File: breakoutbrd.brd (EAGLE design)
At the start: 72.4 x 82.5 mm, 6 parts

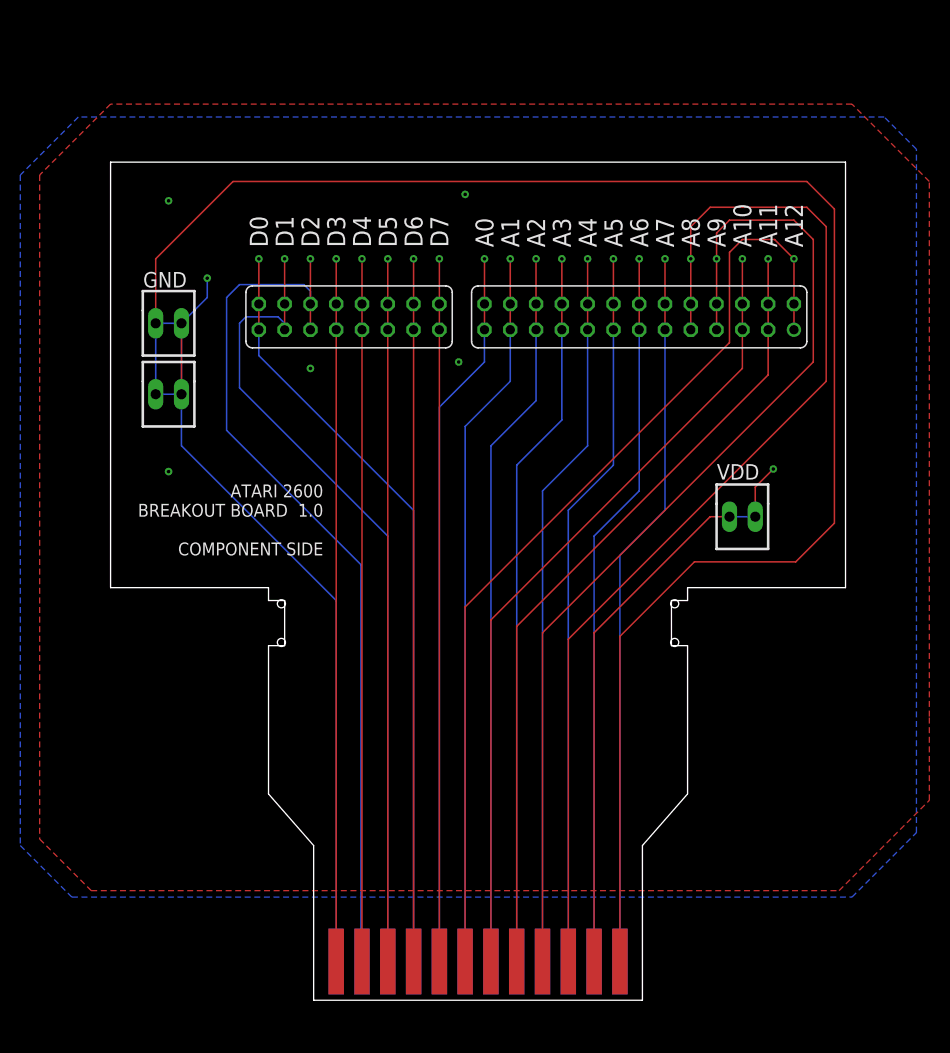
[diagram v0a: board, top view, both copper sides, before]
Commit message: Moved all components to land on 0.1" spacing, even between components. Makes soldering of all pins over a breadboard possible.
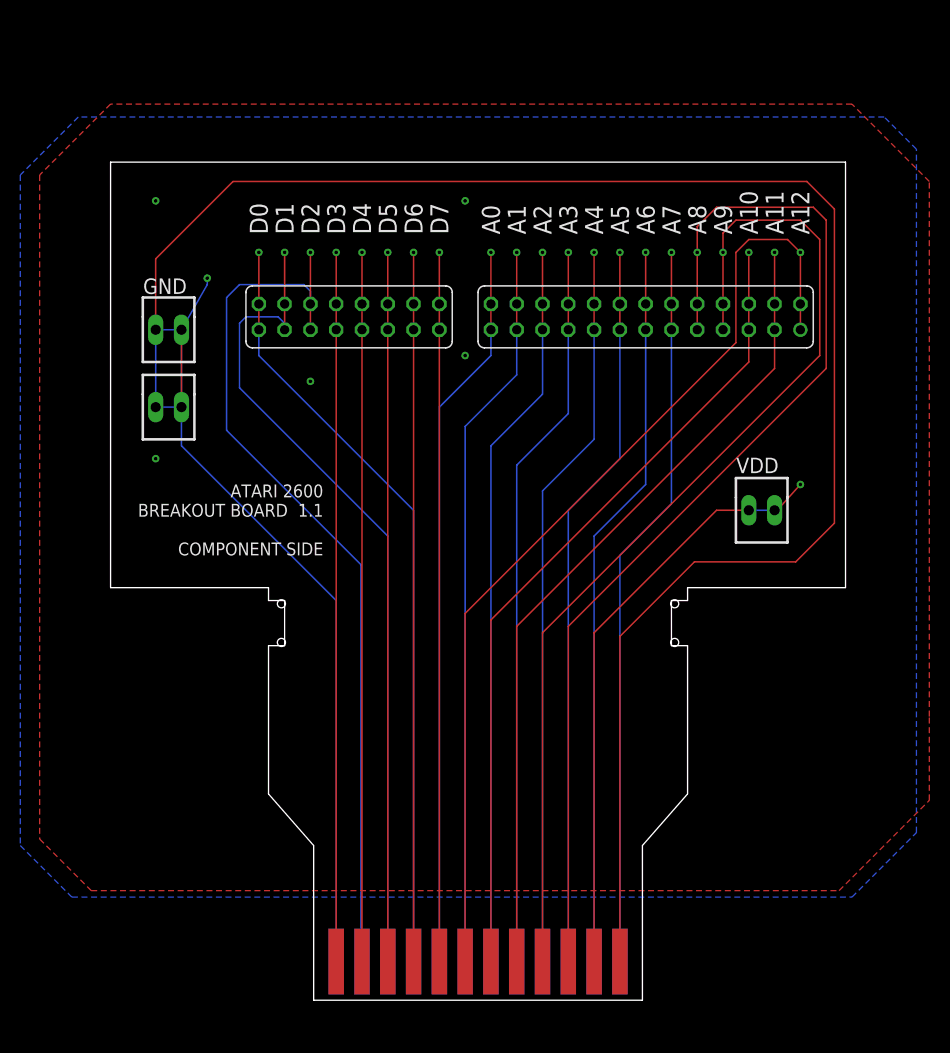
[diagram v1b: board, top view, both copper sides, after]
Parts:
- moved VDD 2.01 mm to (64.8, 48.3)
- moved GND1 1.27 mm to (6.35, 58.4)
- moved SV2 0.64 mm to (53.3, 67.3)
- moved GND 0.63 mm to (6.35, 66.0)
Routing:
- net GND: track 259.9 -> 261.5 mm
- net CADDR7: track 71.1 -> 72.0 mm
- net CADDR6: track 71.1 -> 72.0 mm
- net CADDR11: track 79.5 -> 80.4 mm
- net CADDR10: track 79.5 -> 80.4 mm
- net CADDR5: track 71.1 -> 72.0 mm
- net CADDR4: track 71.1 -> 72.0 mm
- net CADDR2: track 71.1 -> 72.0 mm
- net CADDR1: track 71.1 -> 72.0 mm
- net CADDR0: track 71.1 -> 72.0 mm
- net CADDR3: track 71.1 -> 72.0 mm
- net CADDR12: track 95.3 -> 95.9 mm
- net CDATA7: track 69.2 -> 69.8 mm
- net CDATA6: track 69.2 -> 69.8 mm
- net CDATA5: track 69.2 -> 69.8 mm
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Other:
- board text added: "ATARI 2600 BREAKOUT BOARD 1.1 COMPONENT SIDE"
- board text removed: "ATARI 2600 BREAKOUT BOARD 1.0 COMPONENT SIDE"

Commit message: optional cartridge connector added to pcb
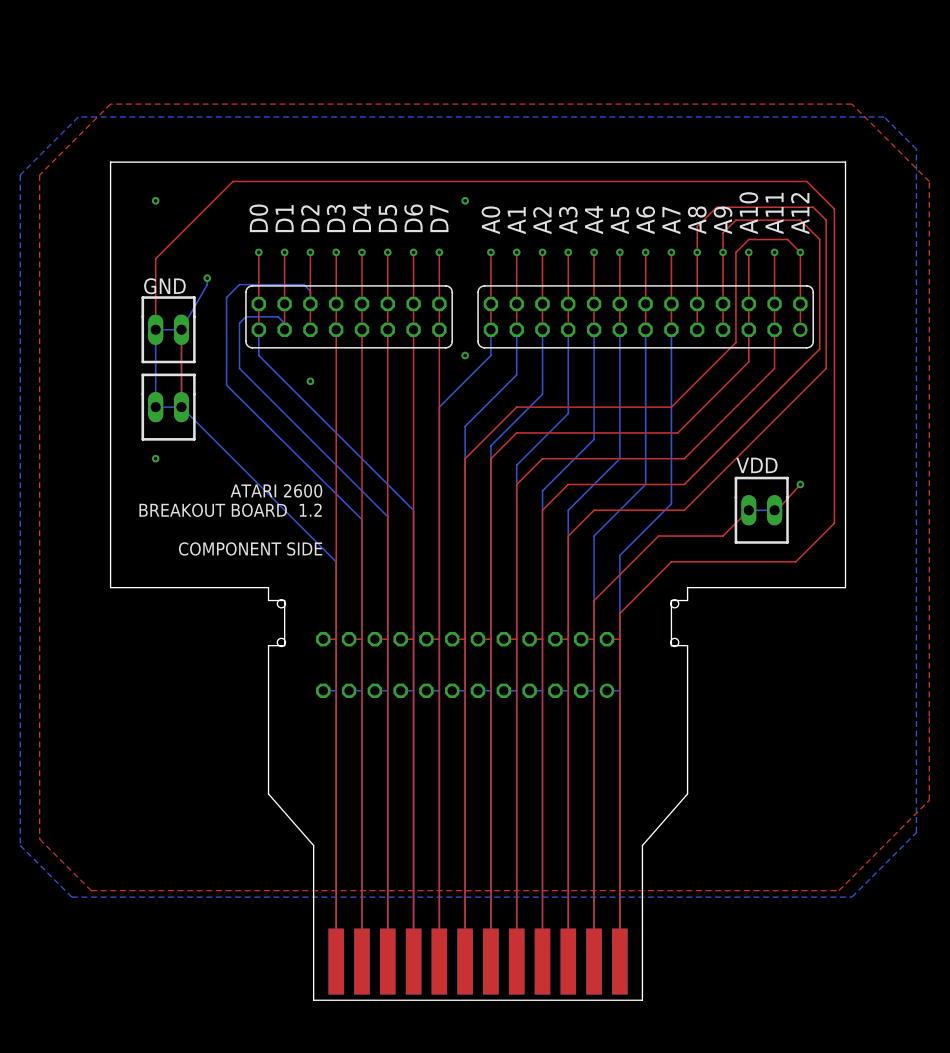
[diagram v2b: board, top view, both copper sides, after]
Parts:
- added U$1: EBC12DCWN, a26board:EBC12DCWN
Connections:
- net CADDR0: now also U$1.8
- net CADDR1: now also U$1.7
- net CADDR10: now also U$1.19
- net CADDR11: now also U$1.20
- net CADDR12: now also U$1.18
- net CADDR2: now also U$1.6
- net CADDR3: now also U$1.5
- net CADDR4: now also U$1.4
- net CADDR5: now also U$1.3
- net CADDR6: now also U$1.2
- net CADDR7: now also U$1.1
- net CADDR8: now also U$1.22
- net CADDR9: now also U$1.21
- net CDATA0: now also U$1.9
- net CDATA1: now also U$1.10
- net CDATA2: now also U$1.11
- net CDATA3: now also U$1.13
- net CDATA4: now also U$1.14
- net CDATA5: now also U$1.15
- net CDATA6: now also U$1.16
- net CDATA7: now also U$1.17
- net GND: now also U$1.12, U$1.24
- net VDD: now also U$1.23
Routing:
- net CADDR10: track 80.4 -> 90.9 mm
- net CADDR12: track 95.9 -> 106.1 mm
- net CADDR11: track 80.4 -> 89.8 mm
- net CADDR9: track 102.8 -> 110.8 mm
- net CADDR8: track 107.7 -> 114.2 mm
- net GND: track 261.5 -> 265.3 mm
- net VDD: track 58.8 -> 62.0 mm
- net CDATA7: track 69.8 -> 71.1 mm
- net CDATA0: track 76.2 -> 77.4 mm
- net CADDR4: track 72.0 -> 73.2 mm
- net CADDR3: track 72.0 -> 73.2 mm
- net CADDR2: track 72.0 -> 73.2 mm
- net CADDR1: track 72.0 -> 73.2 mm
- net CADDR0: track 72.0 -> 73.2 mm
- net CDATA6: track 69.8 -> 71.1 mm
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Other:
- board text added: "ATARI 2600 BREAKOUT BOARD 1.2 COMPONENT SIDE"
- board text added: "CARTRIDGE"
- board text removed: "ATARI 2600 BREAKOUT BOARD 1.1 COMPONENT SIDE"

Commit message: Upright cartridge connector, work in progress
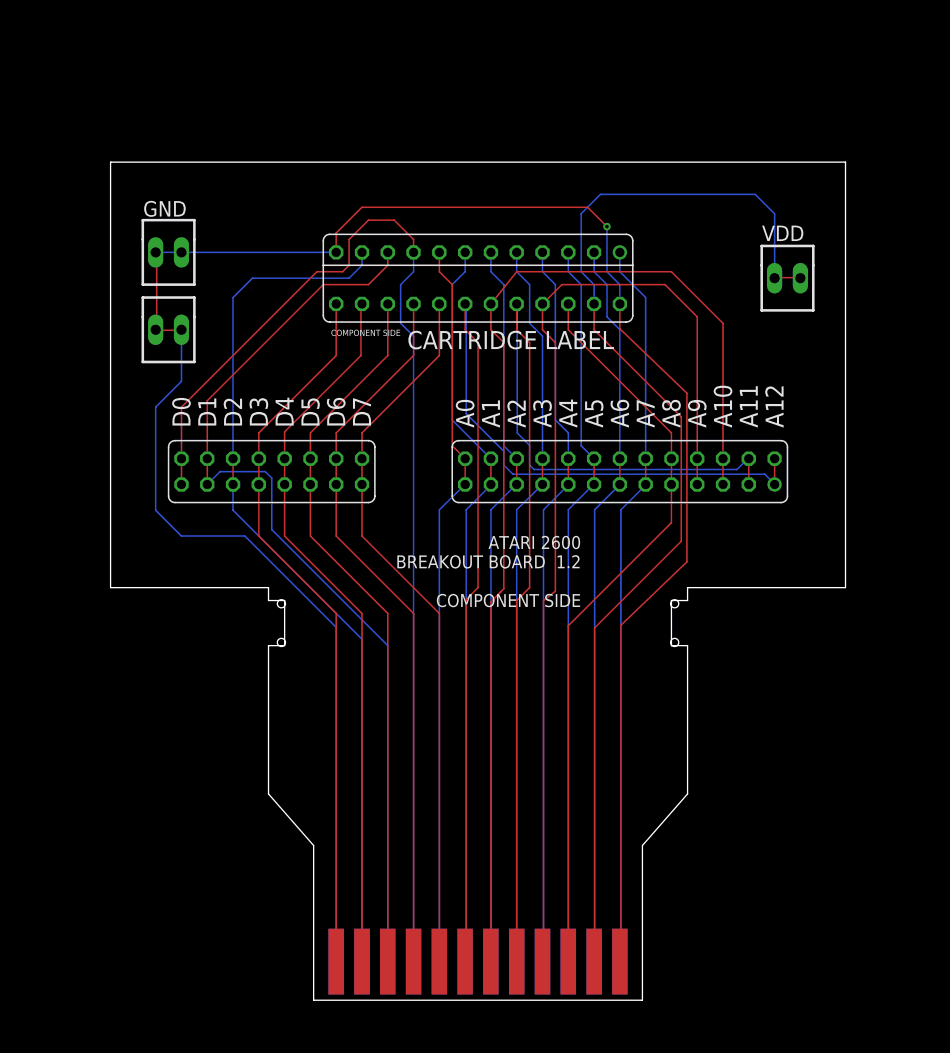
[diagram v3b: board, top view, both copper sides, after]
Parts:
- moved U$1 38.1 mm to (36.8, 71.1), flipped to the top, turned to 180 degrees
- moved VDD 23.0 mm to (67.3, 71.1)
- moved SV1 17.0 mm to (16.5, 52.1)
- moved SV2 15.5 mm to (50.8, 52.1)
- moved GND1 7.62 mm to (6.35, 66.0)
- moved GND 7.62 mm to (6.35, 73.7)
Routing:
- net GND: track 265.3 -> 211.4 mm, vias 6 -> 1
- net VDD: track 62.0 -> 110.9 mm, vias 1 -> 0
- net CADDR8: track 114.2 -> 73.2 mm, vias 1 -> 0
- net CDATA0: track 77.4 -> 112.6 mm, vias 1 -> 0
- net CADDR10: track 90.9 -> 108.6 mm, vias 1 -> 0
- net CADDR11: track 89.8 -> 107.0 mm, vias 1 -> 0
- net CADDR9: track 110.8 -> 99.8 mm, vias 1 -> 0
- net CDATA1: track 83.4 -> 92.3 mm, vias 1 -> 0
- net CADDR12: track 106.1 -> 113.4 mm, vias 1 -> 0
- net CDATA2: track 90.2 -> 86.0 mm, vias 1 -> 0
- net CADDR3: track 73.2 -> 72.0 mm, vias 1 -> 0
- net CADDR0: track 73.2 -> 72.0 mm, vias 1 -> 0
- net CADDR5: track 73.2 -> 72.0 mm, vias 1 -> 0
- net CADDR2: track 73.2 -> 72.0 mm, vias 1 -> 0
- net CADDR6: track 73.2 -> 72.0 mm, vias 1 -> 0
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- removed copper zone on layer 1, net GND
- removed copper zone on layer 16, net GND
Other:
- board text added: "CARTRIDGE LABEL"
- board text removed: "CARTRIDGE"

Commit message: More adjustments
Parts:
- moved VDD 5.08 mm to (67.3, 66.0)
- moved GND1 2.54 mm to (6.35, 63.5)
- moved GND 2.54 mm to (6.35, 71.1)
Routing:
- net CDATA2: track 86.0 -> 81.5 mm
- net VDD: track 110.9 -> 113.4 mm
- net GND: track 211.4 -> 209.7 mm

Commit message: working on double sided edge connectors, work in progrss.
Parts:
- J1: device a26board:MED_NOHOLE -> a26board:BREAKOUT_BOARD
- moved VDD 15.2 mm to (67.3, 50.8)
- moved GND 15.2 mm to (6.35, 55.9)
- moved GND1 15.2 mm to (6.35, 48.3)
- moved SV1 15.2 mm to (16.5, 36.8)
- moved SV2 15.2 mm to (50.8, 36.8)
- moved U$1 15.2 mm to (36.8, 55.9)
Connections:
- net CADDR0: now also J1.32
- net CADDR1: now also J1.31
- net CADDR10: now also J1.43
- net CADDR11: now also J1.44
- net CADDR12: now also J1.42
- net CADDR2: now also J1.30
- net CADDR3: now also J1.29
- net CADDR4: now also J1.28
- net CADDR5: now also J1.27
- net CADDR6: now also J1.26
- net CADDR7: now also J1.25
- net CADDR8: now also J1.46
- net CADDR9: now also J1.45
- net CDATA0: now also J1.33
- net CDATA1: now also J1.34
- net CDATA2: now also J1.35
- net CDATA3: now also J1.37
- net CDATA4: now also J1.38
- net CDATA5: now also J1.39
- net CDATA6: now also J1.40
- net CDATA7: now also J1.41
- net GND: now also J1.36, J1.48
- net VDD: now also J1.47
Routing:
- net GND: track 209.7 -> 179.2 mm
- net VDD: track 113.4 -> 98.1 mm
- net CDATA1: track 92.3 -> 77.1 mm
- net CDATA0: track 112.6 -> 97.3 mm
- net CADDR9: track 99.8 -> 84.6 mm
- net CADDR6: track 72.0 -> 56.7 mm
- net CDATA7: track 71.1 -> 55.8 mm
- net CDATA6: track 71.1 -> 55.8 mm
- net CDATA5: track 71.1 -> 55.8 mm
- net CDATA4: track 71.1 -> 55.9 mm
- net CDATA2: track 81.5 -> 66.2 mm
- net CADDR8: track 73.2 -> 57.9 mm
- net CADDR7: track 72.0 -> 56.8 mm
- net CADDR4: track 72.0 -> 56.8 mm
- net CADDR3: track 72.0 -> 56.7 mm
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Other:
- board size 72.4 x 82.5 mm -> 71.1 x 96.5 mm

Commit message: more layout work
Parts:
- moved VDD 15.2 mm to (67.3, 66.0)
- moved U$1 12.7 mm to (36.8, 68.6)
- moved SV2 10.9 mm to (57.1, 45.7), turned to 270 degrees
- moved GND 10.2 mm to (6.35, 66.0)
- moved GND1 10.2 mm to (6.35, 58.4)
- moved SV1 7.62 mm to (16.5, 44.5), turned to 90 degrees
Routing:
- net GND: track 179.2 -> 257.7 mm
- net CADDR0: track 56.7 -> 116.6 mm, vias 0 -> 2
- net CADDR1: track 57.8 -> 114.1 mm, vias 0 -> 2
- net CADDR2: track 56.7 -> 111.5 mm, vias 0 -> 2
- net CADDR3: track 56.7 -> 109.0 mm, vias 0 -> 2
- net CDATA7: track 55.8 -> 107.7 mm, vias 0 -> 1
- net CADDR4: track 56.8 -> 106.5 mm, vias 0 -> 2
- net CDATA6: track 55.8 -> 105.2 mm, vias 0 -> 1
- net CADDR5: track 56.7 -> 103.9 mm, vias 0 -> 2
- net CDATA5: track 55.8 -> 102.7 mm, vias 0 -> 1
- net CADDR8: track 57.9 -> 102.7 mm, vias 0 -> 1
- net CADDR6: track 56.7 -> 101.4 mm, vias 0 -> 2
- net CDATA4: track 55.9 -> 100.1 mm, vias 0 -> 1
- net CADDR7: track 56.8 -> 98.8 mm, vias 0 -> 2
- net CDATA3: track 55.8 -> 97.6 mm, vias 0 -> 1
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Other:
- board text added: "ATARI 2600 BREAKOUT BOARD 2.0 COMPONENT SIDE"
- board text removed: "ATARI 2600 BREAKOUT BOARD 1.2 COMPONENT SIDE"

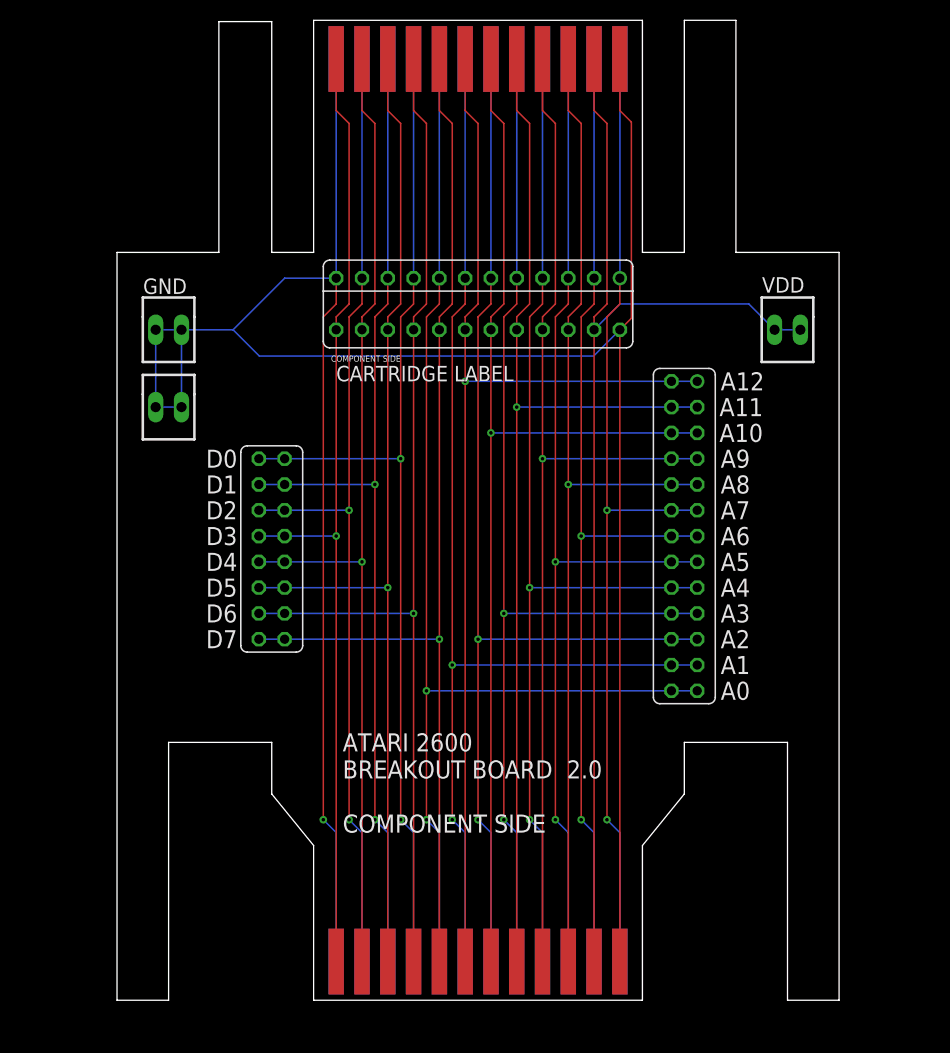
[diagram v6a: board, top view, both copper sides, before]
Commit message: spread out vias grouped VDD and GND points on same side better labeling
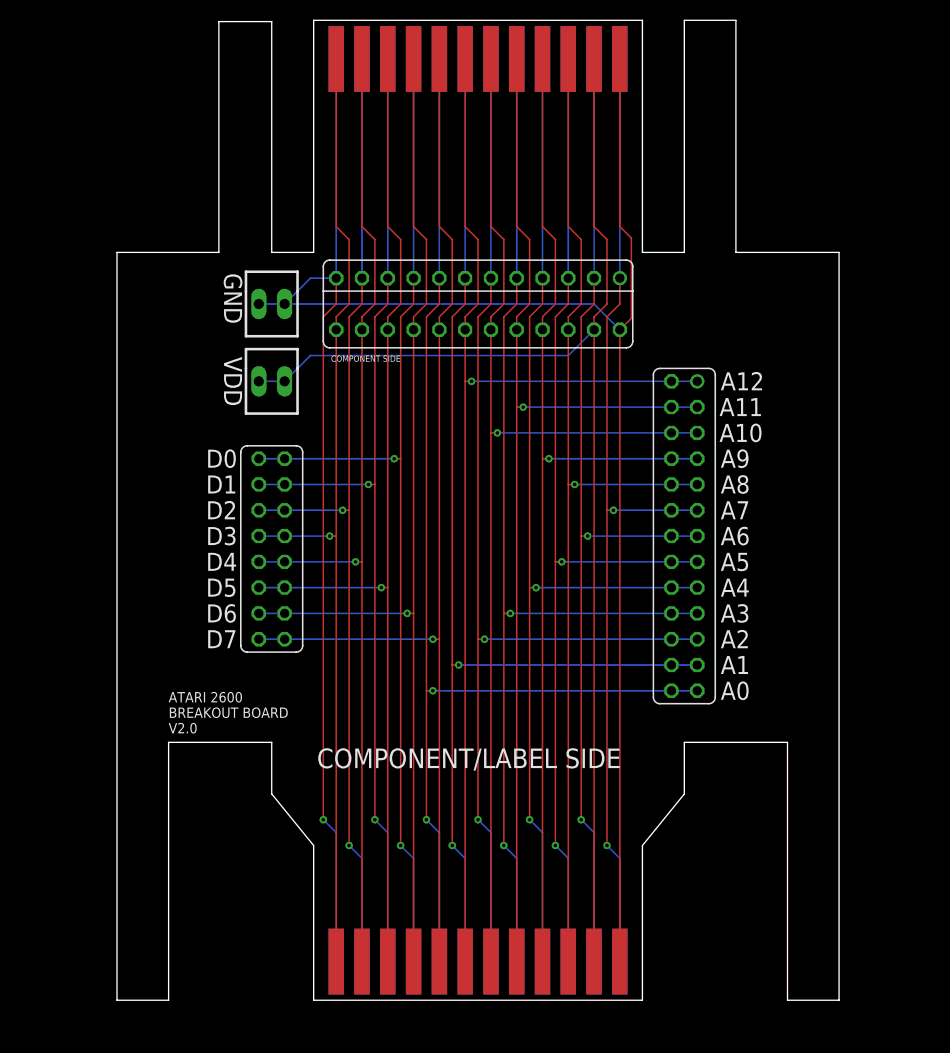
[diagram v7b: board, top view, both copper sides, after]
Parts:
- removed GND: 22-23-2021, a26board:22-23-2021
- moved VDD 51.1 mm to (16.5, 61.0)
- moved GND1 14.4 mm to (16.5, 68.6)
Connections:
- net GND: no longer GND.1, GND.2
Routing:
- net GND: track 257.7 -> 222.5 mm
- net VDD: track 112.4 -> 125.1 mm
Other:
- board text added: "ATARI 2600 BREAKOUT BOARD V2.0"
- board text added: "COMPONENT/LABEL SIDE"
- board text removed: "ATARI 2600 BREAKOUT BOARD 2.0 COMPONENT SIDE"
- board text removed: "CARTRIDGE LABEL"

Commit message: Cartridge extension, prongs measured.
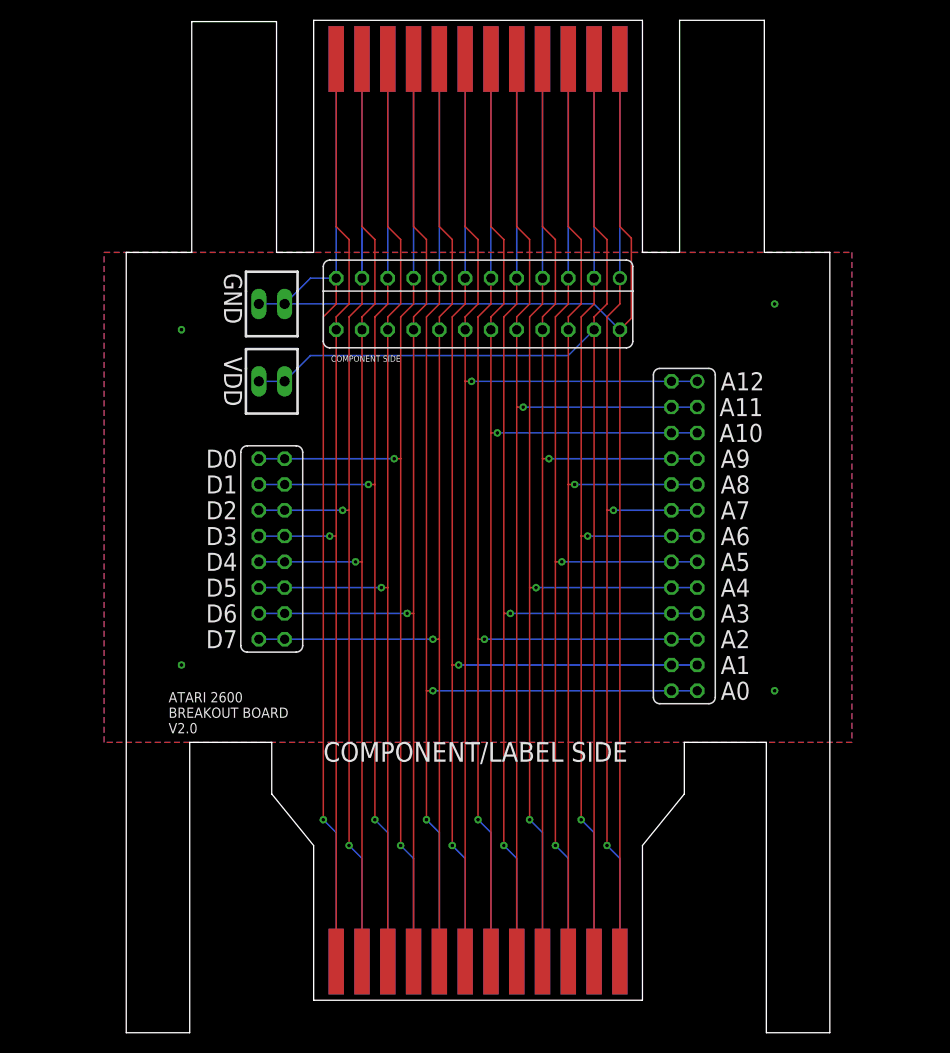
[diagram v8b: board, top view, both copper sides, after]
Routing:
- net GND: vias 1 -> 5
- added copper zone on layer 1, net GND
- added copper zone on layer 16, net GND
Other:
- board size 71.1 x 96.5 mm -> 69.3 x 99.7 mm
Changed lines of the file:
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@@
 <board>
 <plain>
-<text x="20.955" y="22.86" size="1.9304" layer="21" font="vector">COMPONENT/LABEL SIDE
+<text x="21.59" y="23.495" size="1.9304" layer="21" font="vector">COMPONENT/LABEL SIDE
 </text>
 <text x="10.033" y="52.451" size="1.778" layer="21">D0</text>
@@
 <wire x1="48.26" y1="68.58" x2="50.8" y2="66.04" width="0.1524" layer="16"/>
 <wire x1="17.78" y1="68.58" x2="20.32" y2="71.12" width="0.1524" layer="16"/>
+<polygon width="0.1524" layer="16">
+<vertex x="0" y="25.4"/>
+<vertex x="0" y="73.66"/>
+<vertex x="73.66" y="73.66"/>
+<vertex x="73.66" y="25.4"/>
+</polygon>
+<polygon width="0.1524" layer="1">
+<vertex x="0" y="25.4"/>
+<vertex x="0" y="73.66"/>
+<vertex x="73.66" y="73.66"/>
+<vertex x="73.66" y="25.4"/>
+</polygon>
+<via x="7.62" y="66.04" extent="1-16" drill="0.35"/>
+<via x="7.62" y="33.02" extent="1-16" drill="0.35"/>
+<via x="66.04" y="68.58" extent="1-16" drill="0.35"/>
+<via x="66.04" y="30.48" extent="1-16" drill="0.35"/>
 </signal>
 <signal name="VDD">
